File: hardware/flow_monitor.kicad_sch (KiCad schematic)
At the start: 59 parts, among them J1 Conn_01x07_Pin, J5 Conn_01x02_Socket_TOP, J7 Conn_01x02_Socket_BOT, J8 Conn_01x06_Socket, Q1 2N7002, Q3 AO3401A, Q5 2N7002, Q6 2N7002, SW2 1TS005F-2500-5001, SW4 1TS005F-2500-5001, SW5 SK12D07VG5, U4 TPS610982DSET, U6 STM32G030C8Tx, U7 EA_DOGS164W-A, Y1 Crystal

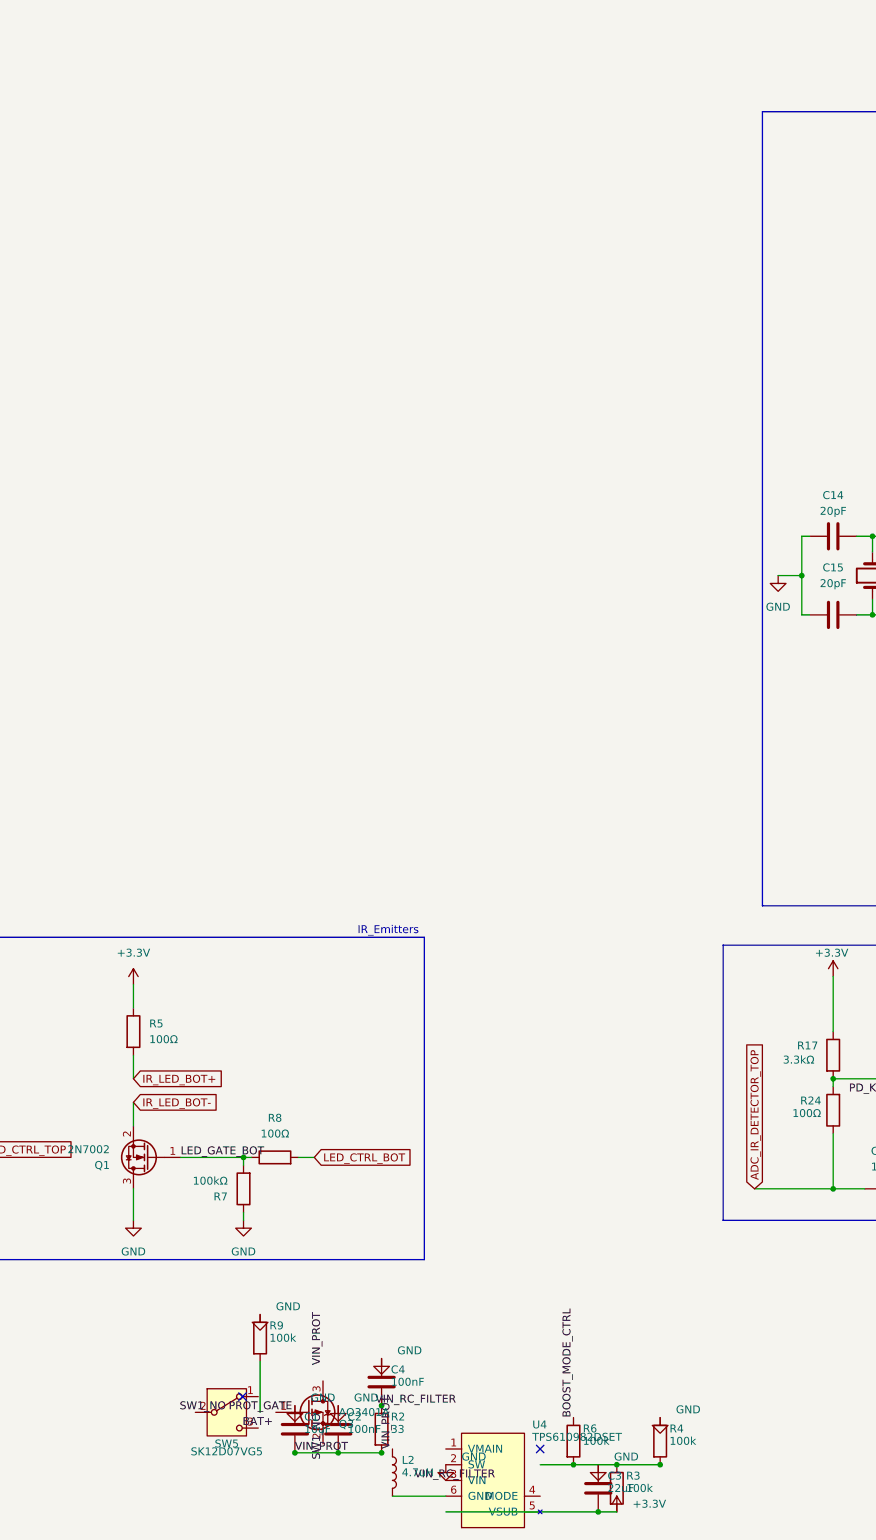
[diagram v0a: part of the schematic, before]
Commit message: bom: update L2 to Murata DFE201612E-4R7M=P2
Replace Sunlord MPL2016S4R7MHT (no DigiKey stock, unlisted Isat,
non-qualified supplier) with Murata DFE201612E-4R7M=P2.
Same 2016/0806 footprint, 4.7uH, DCR 252mΩ, Isat 1.8A.
Active lifecycle, stocked at DigiKey/Mouser/Newark.

Co-Authored-By: Claude Sonnet 4.6 <noreply@anthropic.com>
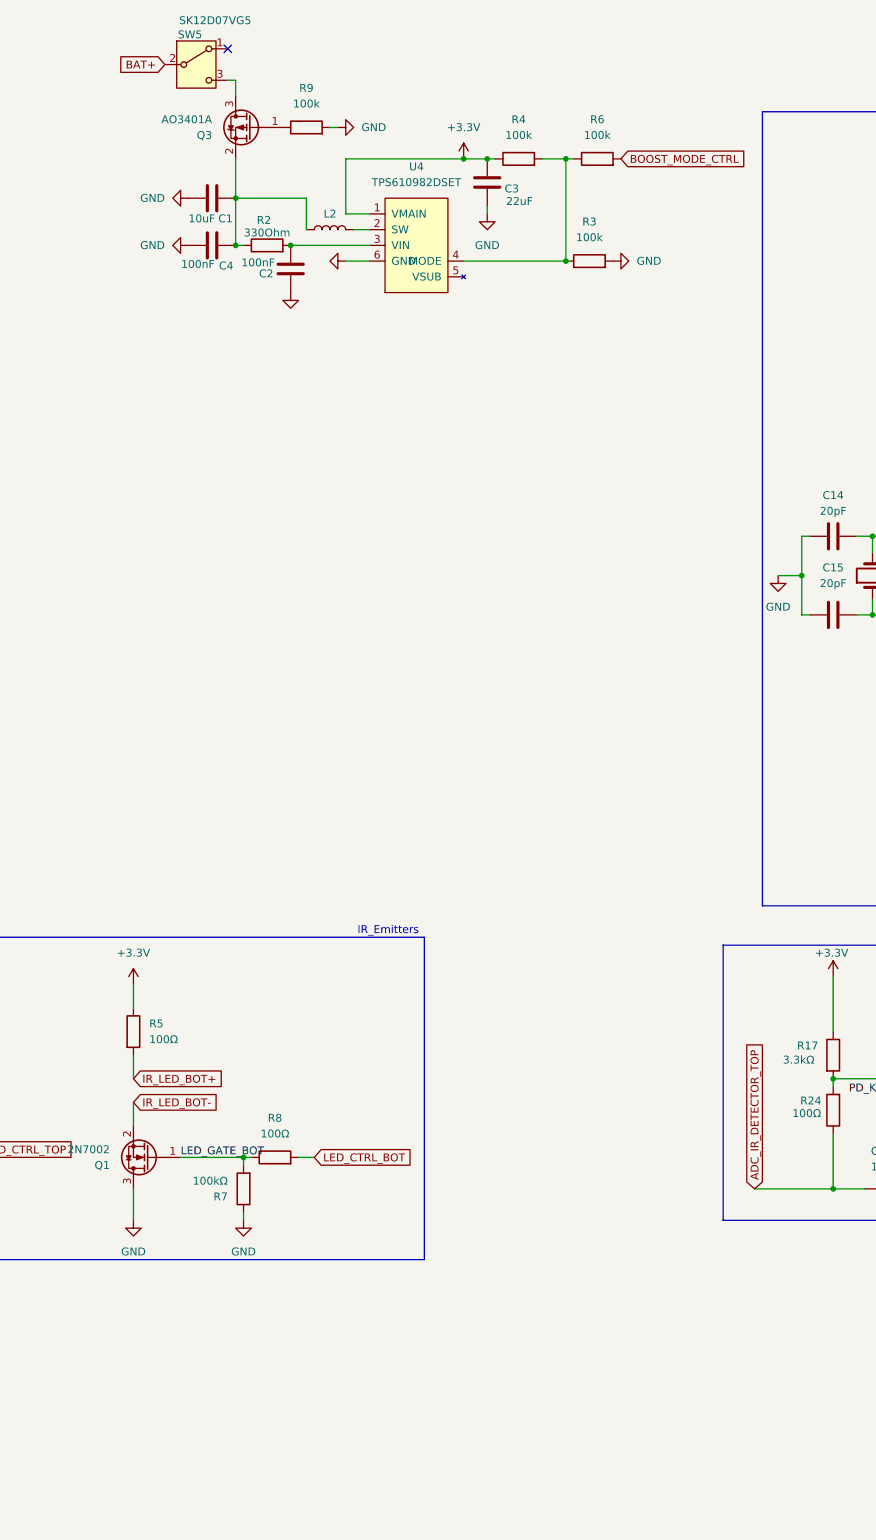
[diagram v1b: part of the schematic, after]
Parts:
- L2: MPN MPL2016S4R7MHT -> DFE201612E-4R7M=P2
- R2: value 33 -> 330Ohm
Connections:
- net +3.3V: now also R4.1, U4.1 (VMAIN); no longer R3.2
- net BAT+: now also SW5.2 (B)
- net BOOST_MODE_CTRL: now also R6.2; no longer R6.1
- net GND: now also C1.2, R3.2, R9.2, U4.6 (GND); no longer C1.1, R4.1, R9.1, U4.2 (SW)
- net at Q3.1 (G): now also R9.1
- net at Q3.2 (S): now also C1.1, C4.2, L2.1, R2.1
- net at Q3.3 (D): now also SW5.3 (C)
- net at L2.2: now also U4.2 (SW); no longer U4.6 (GND)
- net at U4.3 (VIN): now also C2.2, R2.2
- net at U4.4 (MODE): now also R3.1, R4.2, R6.1
- removed net VIN_PROT: C1.2, C2.2, L2.1, R2.2
- no-connect marks 27 -> 26
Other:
- moved on the sheet: C1, C2, C3, C4, L2, Q3, R2, R3, R4, R6, R9, SW5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
